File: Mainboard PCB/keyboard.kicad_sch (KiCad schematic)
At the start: 157 parts, among them J1 HRO_TYPE-C-31-M-12, J2 Conn_01x03, SW1 Alps SKRK, SW2 Alps SKRK, U1 TLV75533PDBV, U101 RP2040, U103 W25Q16, Y1 12MHz 3225

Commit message: routed all traces needed thus far among other things required
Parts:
- removed C10, C13, C9: 100nF 0402, Capacitor_SMD:C_0402_1005Metric, symbol Device:C_Small
- added H1, H2, H3, H4: MountingHole, MountingHole:MountingHole_3.5mm_Pad, symbol Mechanical:MountingHole
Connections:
- net col0: now also U101.6 (GPIO4)
- net col1: now also U101.7 (GPIO5)
- net col10: now also U101.30 (GPIO19)
- net col11: now also U101.31 (GPIO20)
- net col12: now also U101.32 (GPIO21)
- net col13: now also U101.34 (GPIO22)
- net col2: now also U101.8 (GPIO6)
- net col3: now also U101.9 (GPIO7)
- net col4: now also U101.11 (GPIO8)
- net col5: now also U101.12 (GPIO9)
- net col6: now also U101.13 (GPIO10)
- net col7: now also U101.27 (GPIO16)
- net col8: now also U101.28 (GPIO17)
- net col9: now also U101.29 (GPIO18)
- net row0: now also U101.14 (GPIO11); no longer U101.2 (GPIO0)
- net row1: now also U101.15 (GPIO12); no longer U101.3 (GPIO1)
- net row2: now also U101.16 (GPIO13); no longer U101.4 (GPIO2)
- net row3: now also U101.17 (GPIO14); no longer U101.5 (GPIO3)
- net row4: now also U101.18 (GPIO15); no longer U101.6 (GPIO4)
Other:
- moved on the sheet: C11, C12, C5, C6, C7, C8

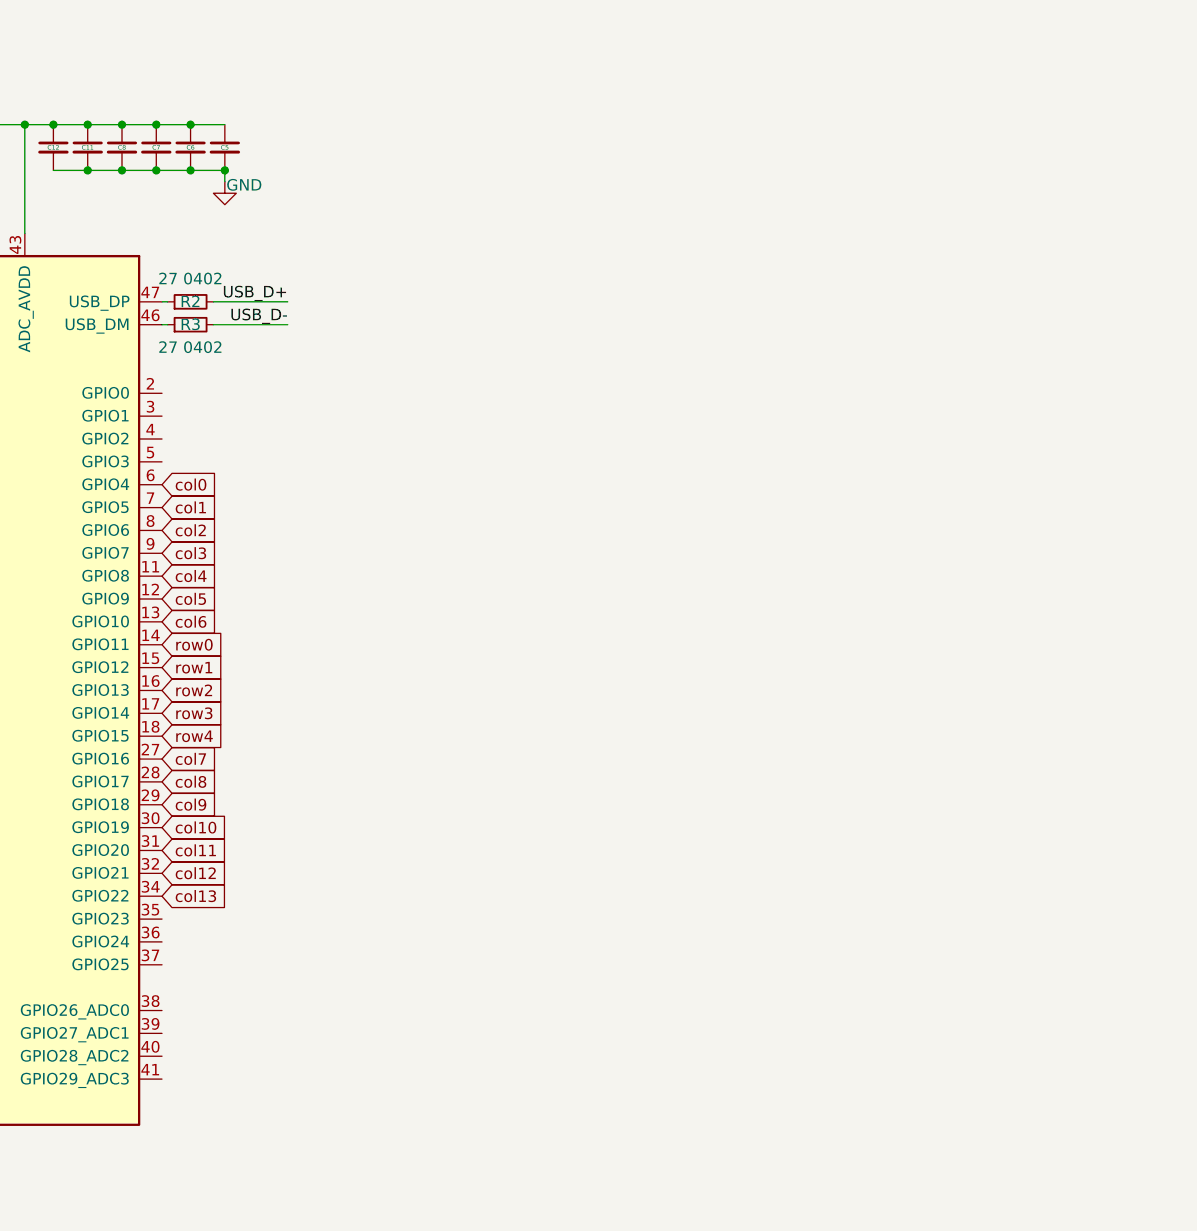
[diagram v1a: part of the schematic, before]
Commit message: added power circuit for solenoids
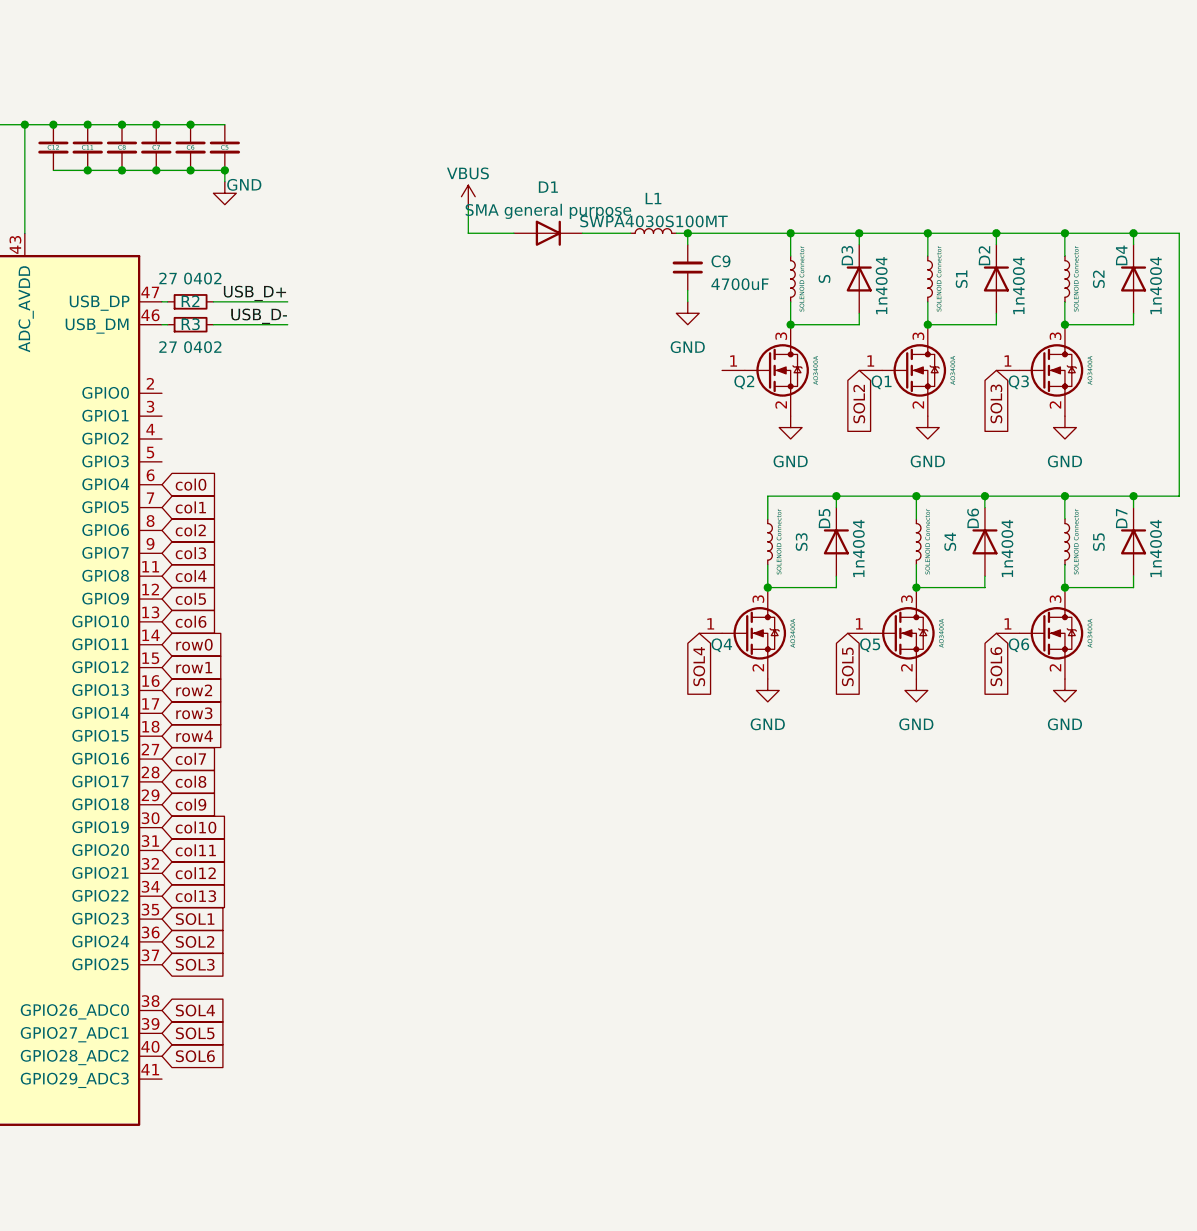
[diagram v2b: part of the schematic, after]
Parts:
- added C9: 4700uF, symbol Device:C_Small
- added D1: SMA general purpose, Diode_THT:D_DO-201AD_P15.24mm_Horizontal, symbol Diode:1N5400
- added D2, D3, D4, D5, D6, D7: 1n4004, Diode_THT:D_DO-41_SOD81_P10.16mm_Horizontal, symbol Diode:1N4004
- added L1: SWPA4030S100MT, Inductor_SMD:L_Sunlord_SWPA4030S, symbol Device:L_Small
- added Q1, Q2, Q3, Q4, Q5, Q6: AO3400A, Package_TO_SOT_SMD:SOT-23, symbol Transistor_FET:AO3400A
- added S, S1, S2, S3, S4, S5: SOLENOID Connector, Connector_PinHeader_2.54mm:PinHeader_1x01_P2.54mm_Vertical, symbol Device:L_Small
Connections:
- net GND: now also C9.1, Q1.2 (S), Q2.2 (S), Q3.2 (S), Q4.2 (S), Q5.2 (S), Q6.2 (S)
- net VBUS: now also D1.2 (A)
- net SOL1: now reaches U101.35 (GPIO23)
- net SOL2: now reaches U101.36 (GPIO24)
- net SOL2: now also Q1.1 (G)
- net SOL3: now reaches U101.37 (GPIO25)
- net SOL3: now also Q3.1 (G)
- net SOL4: now reaches U101.38 (GPIO26_ADC0)
- net SOL4: now also Q4.1 (G)
- net SOL5: now reaches U101.39 (GPIO27_ADC1)
- net SOL5: now also Q5.1 (G)
- net SOL6: now reaches U101.40 (GPIO28_ADC2)
- net SOL6: now also Q6.1 (G)
- new net: C9.2, D2.1 (K), D3.1 (K), D4.1 (K), D5.1 (K), D6.1 (K), D7.1 (K), L1.2, S.1, S1.1, S2.1, S3.1, S4.1, S5.1
- new net: D6.2 (A), Q5.3 (D), S4.2
- new net: D2.2 (A), Q1.3 (D), S1.2
- new net: D7.2 (A), Q6.3 (D), S5.2
- new net: D5.2 (A), Q4.3 (D), S3.2
- new net: D3.2 (A), Q2.3 (D), S.2
- new net: D1.1 (K), L1.1
- new net: D4.2 (A), Q3.3 (D), S2.2

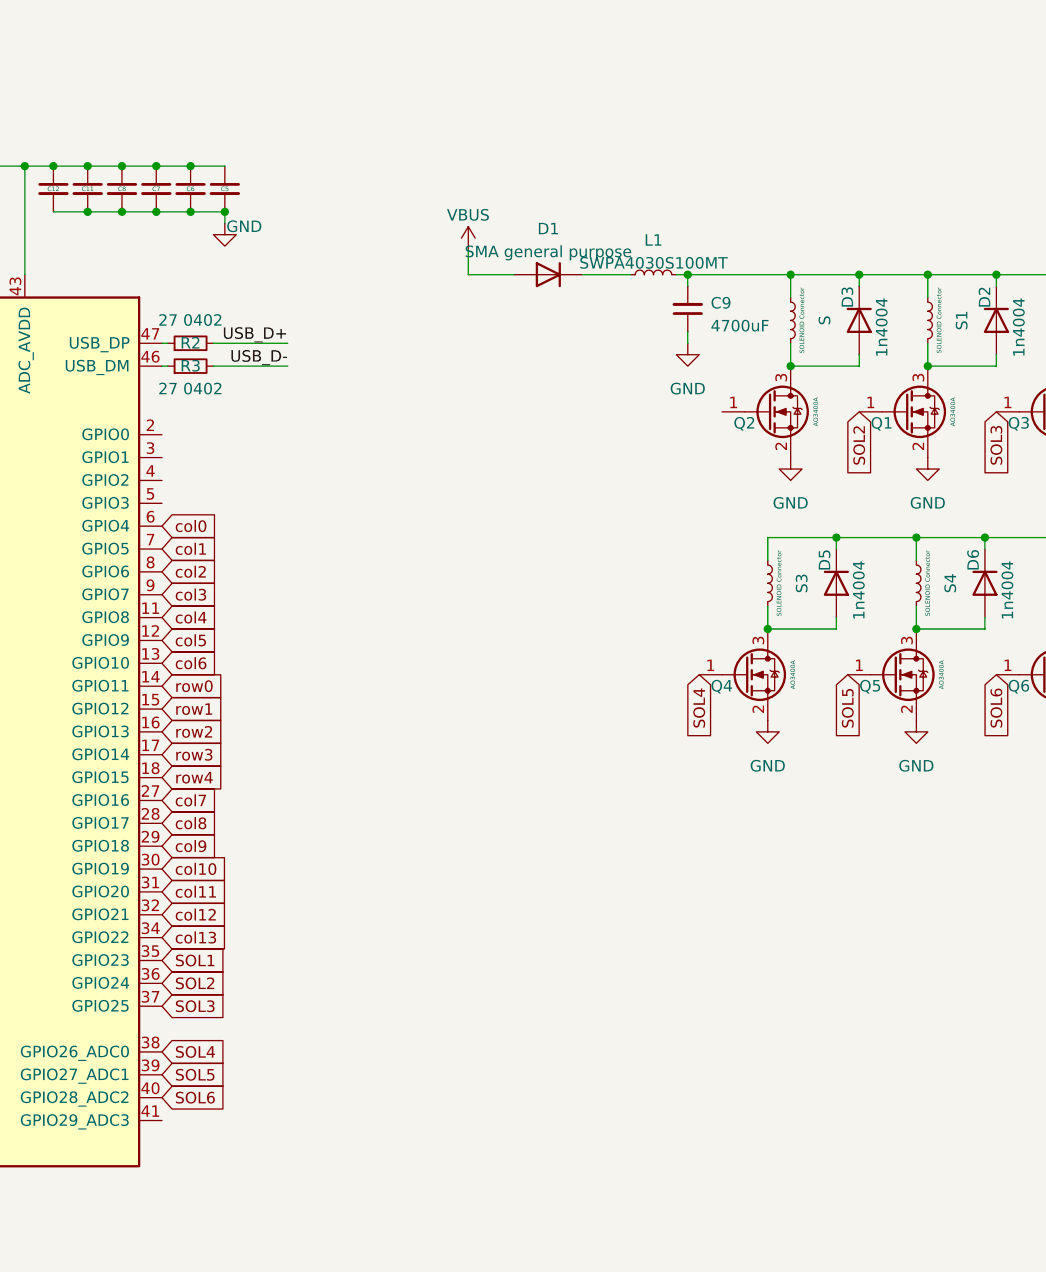
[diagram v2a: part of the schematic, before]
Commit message: added power circuitry for 6 solenoids
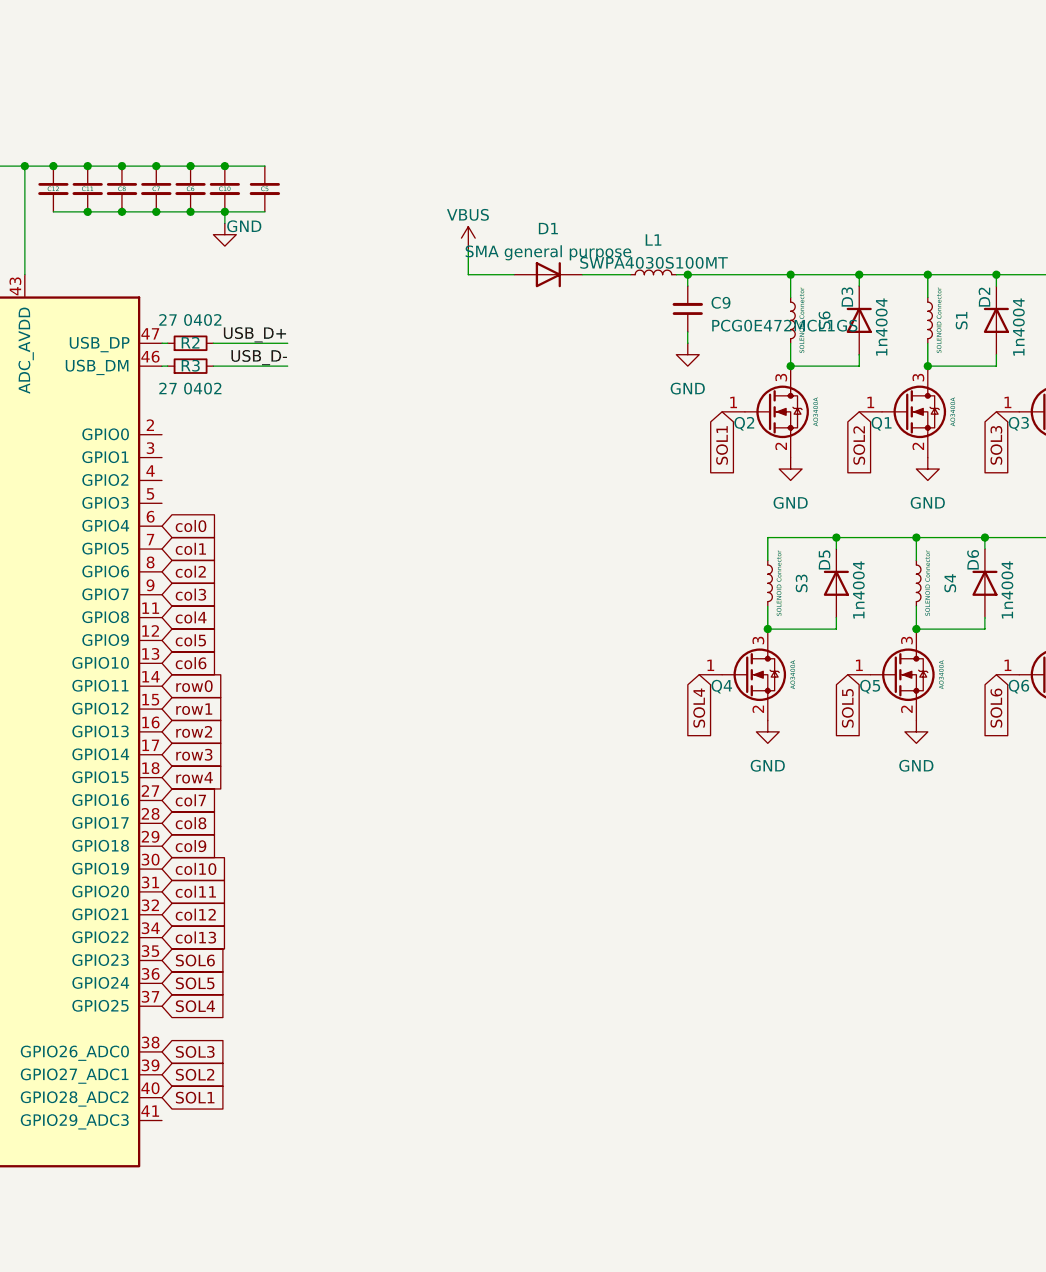
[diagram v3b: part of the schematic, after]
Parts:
- added C10: 100nF 0402, Capacitor_SMD:C_0402_1005Metric, symbol Device:C_Small
- C9: value 4700uF -> PCG0E472MCL1GS; footprint (none) -> Capacitor_SMD:CP_Elec_10x12.6
- D1: footprint Diode_THT:D_DO-201AD_P15.24mm_Horizontal -> Diode_SMD:D_SMA
- D2, D3, D4, D5, D6, D7: footprint Diode_THT:D_DO-41_SOD81_P10.16mm_Horizontal -> Diode_SMD:D_SMA
- S1, S2, S3, S4, S5: footprint Connector_PinHeader_2.54mm:PinHeader_1x01_P2.54mm_Vertical -> Connector_PinHeader_2.54mm:PinHeader_1x02_P2.54mm_Vertical
- S6: renamed from S; footprint Connector_PinHeader_2.54mm:PinHeader_1x01_P2.54mm_Vertical -> Connector_PinHeader_2.54mm:PinHeader_1x02_P2.54mm_Vertical
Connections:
- net +3V3: now also C10.1
- net GND: now also C10.2
- net SOL1: now also Q2.1 (G), U101.40 (GPIO28_ADC2); no longer U101.35 (GPIO23)
- net SOL2: now also U101.39 (GPIO27_ADC1); no longer U101.36 (GPIO24)
- net SOL3: now also U101.38 (GPIO26_ADC0); no longer U101.37 (GPIO25)
- net SOL4: now also U101.37 (GPIO25); no longer U101.38 (GPIO26_ADC0)
- net SOL5: now also U101.36 (GPIO24); no longer U101.39 (GPIO27_ADC1)
- net SOL6: now also U101.35 (GPIO23); no longer U101.40 (GPIO28_ADC2)
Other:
- moved on the sheet: C5

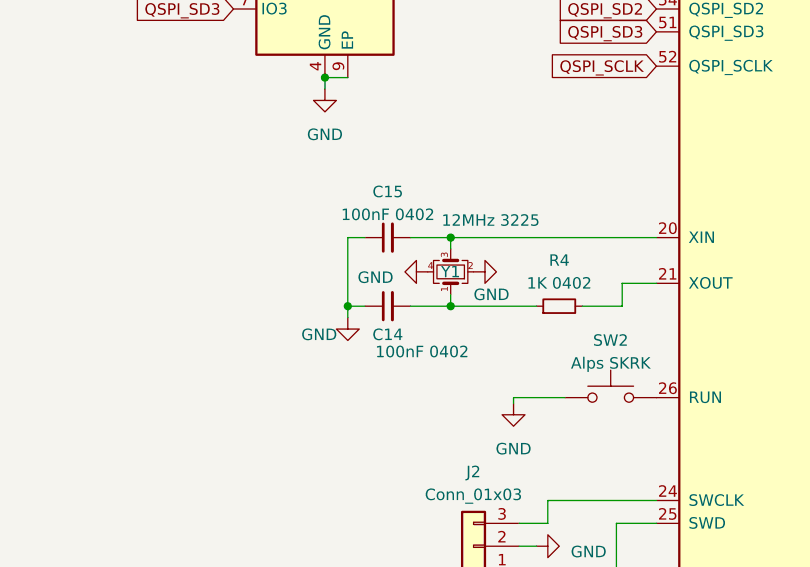
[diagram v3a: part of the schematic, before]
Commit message: added correct sized cap and generated gerber + BOM
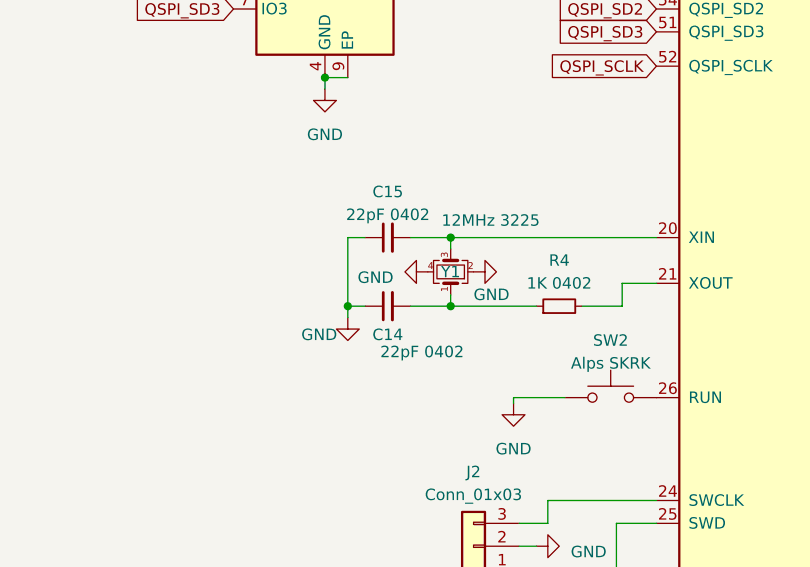
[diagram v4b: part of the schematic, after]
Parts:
- C14, C15: value 100nF 0402 -> 22pF 0402
- C9: footprint Capacitor_SMD:CP_Elec_10x12.6 -> Capacitor_SMD:CP_Elec_18x17.5
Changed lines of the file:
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@@
       (effects (font (size 1.27 1.27)) (justify right))
     )
-    (property "Footprint" "Capacitor_SMD:CP_Elec_10x12.6" (at 340.36 175.26 0)
+    (property "Footprint" "Capacitor_SMD:CP_Elec_18x17.5" (at 340.36 175.26 0)
       (effects (font (size 1.27 1.27)) hide)
     )
@@
       (effects (font (size 1.27 1.27)))
     )
-    (property "Value" "100nF 0402" (at 192.405 237.49 90)
+    (property "Value" "22pF 0402" (at 192.405 237.49 90)
       (effects (font (size 1.27 1.27)))
     )
@@
       (effects (font (size 1.27 1.27)))
     )
-    (property "Value" "100nF 0402" (at 188.6013 222.25 90)
+    (property "Value" "22pF 0402" (at 188.6013 222.25 90)
       (effects (font (size 1.27 1.27)))
     )
